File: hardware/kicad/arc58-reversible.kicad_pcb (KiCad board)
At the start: 2 copper layers, 169.3 x 152.2 mm, 91 parts, among them J1 MJ-4PP-9_Reversible, J2 SSD1306 OLED 128x32, SW1 SW_PUSH_LED, SW10 SW_PUSH_LED, SW11 SW_PUSH_LED, SW12 SW_PUSH_LED, SW13 SW_PUSH_LED, SW14 SW_PUSH_LED, SW15 SW_PUSH_LED, SW16 SW_PUSH_LED, SW17 SW_PUSH_LED, SW18 SW_PUSH_LED, SW19 SW_PUSH_LED, SW2 SW_PUSH_LED, SW20 SW_PUSH_LED, SW21 SW_PUSH_LED, SW22 SW_PUSH_LED, SW23 SW_PUSH_LED, SW24 SW_PUSH_LED, SW25 Rotary_Encoder_Switch, SW26 SW_PUSH_LED, SW27 SW_PUSH_LED, SW28 SW_PUSH_LED, SW29 SW_PUSH_LED, SW3 SW_PUSH_LED, SW4 SW_PUSH_LED, SW5 SW_PUSH_LED, SW6 SW_PUSH_LED, SW7 SW_PUSH_LED, SW8 SW_PUSH_LED, SW9 SW_PUSH_LED, U1 KEEBD Helios RP2040, U2 74AHCT1G125

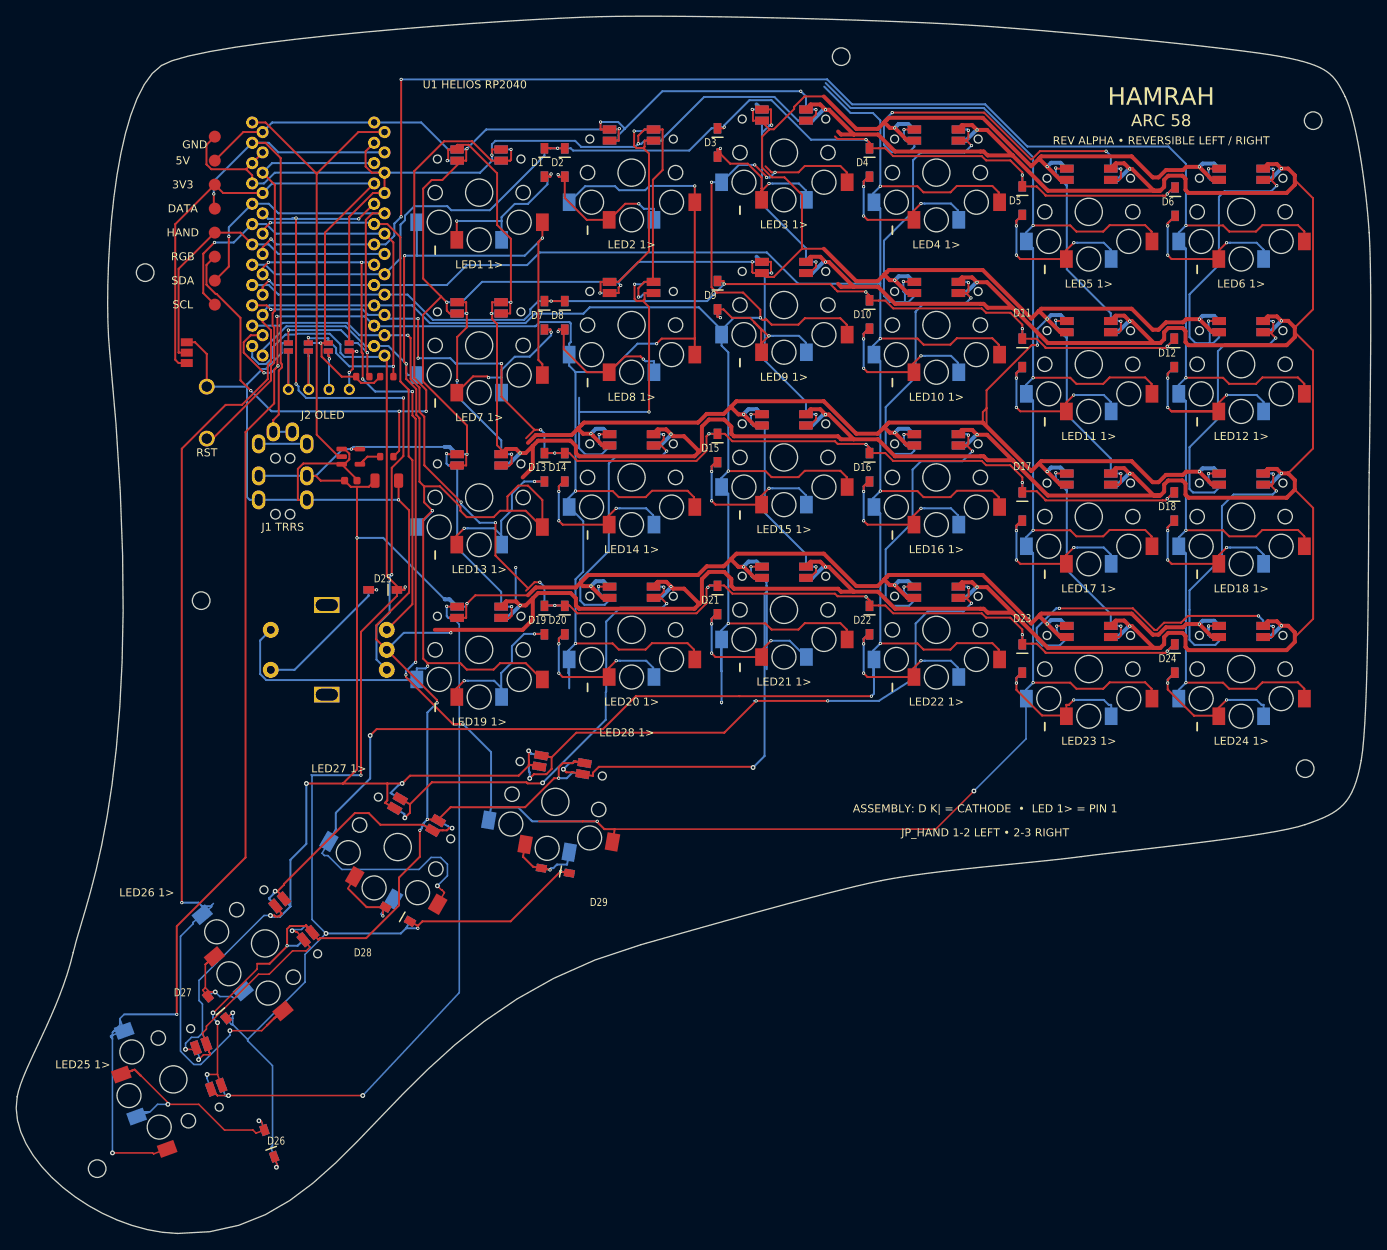
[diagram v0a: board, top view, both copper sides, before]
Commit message: Fix RGB apertures and TRRS clearance
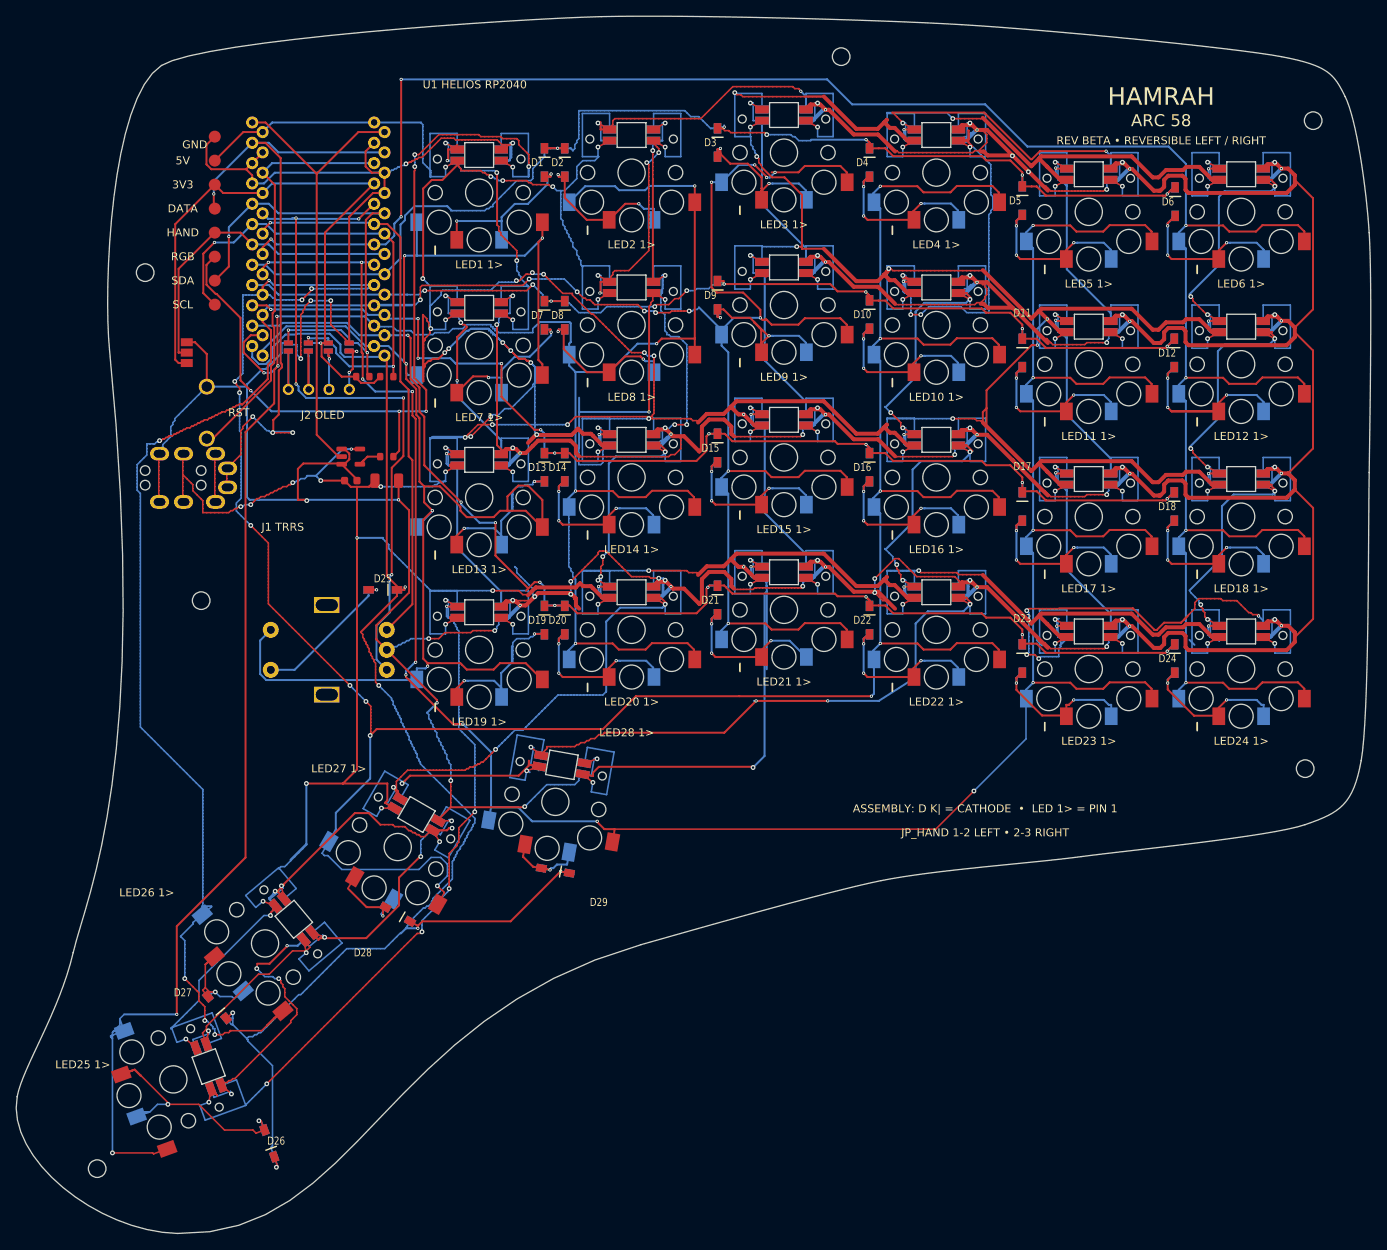
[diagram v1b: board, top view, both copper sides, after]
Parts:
- moved J1 12.7 mm to (83.3, 85.7), turned to 0 degrees
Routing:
- net VBUS: track 843.4 -> 1307.4 mm, vias 32 -> 73
- net GND: track 1032.1 -> 1181.9 mm, vias 35 -> 82
- net COL1: track 356.4 -> 310.9 mm
- net Net-(SW23-Pad2): track 45.4 -> 76.8 mm, vias 4 -> 7
- net Net-(SW10-Pad2): track 42.2 -> 71.2 mm, vias 3 -> 5
- net Net-(SW27-Pad2): track 36.5 -> 57.0 mm, vias 2 -> 4
- net RGB_LED_IN: track 96.4 -> 116.3 mm, vias 4 -> 7
- net Net-(SW14-Pad2): track 45.5 -> 64.1 mm, vias 3 -> 4
- net Net-(SW15-Pad2): track 27.7 -> 45.6 mm, vias 2 -> 3
- net Net-(SW11-Pad2): track 29.3 -> 46.3 mm, vias 2 -> 3
- net Net-(SW11-Pad4): track 29.3 -> 46.4 mm, vias 2 -> 3
- net Net-(SW17-Pad2): track 29.3 -> 46.3 mm, vias 2 -> 3
- net Net-(SW13-Pad2): track 27.9 -> 44.9 mm, vias 2 -> 3
- net SPLIT_DATA: track 68.8 -> 85.3 mm, vias 1 -> 4
- net Net-(SW1-Pad2): track 31.7 -> 47.7 mm, vias 2 -> 5
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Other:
- board text added: "REV BETA • REVERSIBLE LEFT / RIGHT"
- board text removed: "REV ALPHA • REVERSIBLE LEFT / RIGHT"

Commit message: Fix reversible thumb switch axes
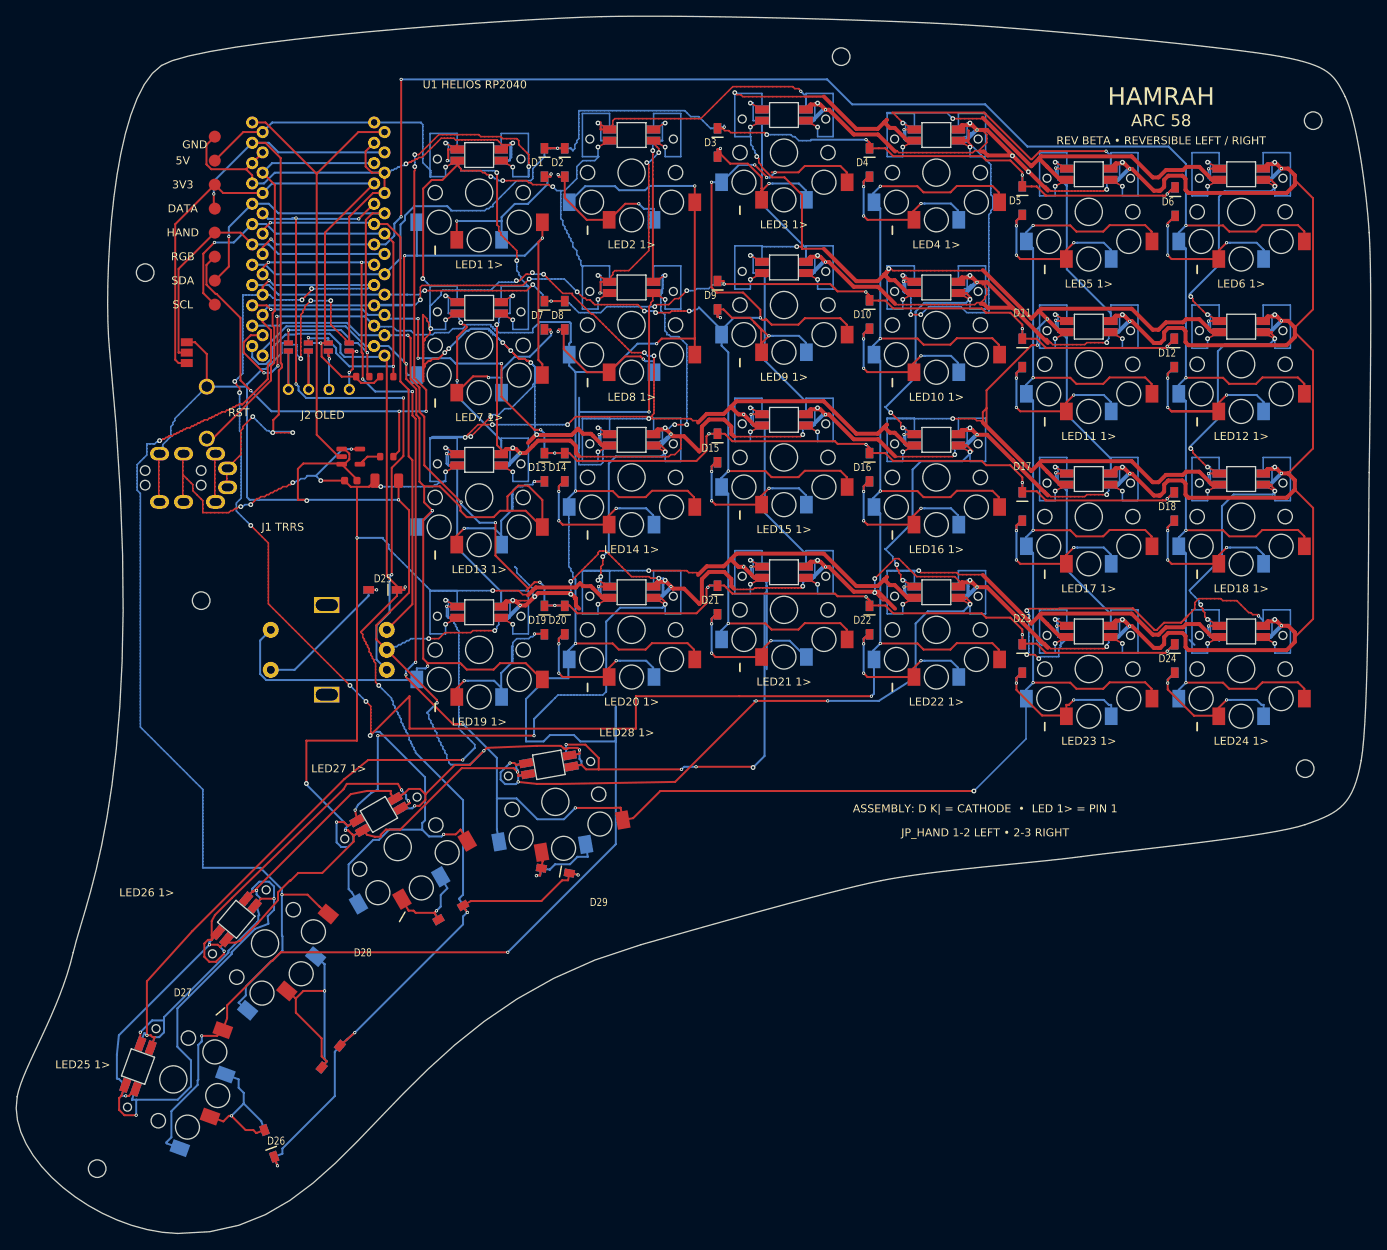
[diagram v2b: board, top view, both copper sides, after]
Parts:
- moved D27 15.5 mm to (102.0, 158.0), turned to -130 degrees
- moved D28 6.63 mm to (117.0, 140.0), turned to -150 degrees
- turned SW26 to -110 degrees
- turned SW27 to -130 degrees
- turned SW28 to -150 degrees
- turned SW29 to -170 degrees
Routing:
- net VBUS: track 1307.4 -> 1268.3 mm, vias 73 -> 71
- net ROW4: track 187.6 -> 168.7 mm
- net Net-(D26-Pad2): track 38.1 -> 19.7 mm, vias 2 -> 1
- net Net-(D27-Pad2): track 14.2 -> 30.7 mm
- net Net-(SW20-Pad4): track 76.0 -> 89.9 mm, vias 3 -> 5
- net Net-(SW26-Pad2): track 42.6 -> 56.0 mm
- net Net-(SW19-Pad2): track 103.3 -> 90.9 mm, vias 7 -> 4
- net Net-(SW27-Pad2): track 57.0 -> 47.8 mm, vias 4 -> 3
- net Net-(SW21-Pad2): track 83.5 -> 74.5 mm, vias 4 -> 6
- net GND: track 1181.9 -> 1175.4 mm, vias 82 -> 77
- net COL3: track 333.7 -> 327.7 mm, vias 17 -> 15
- net Net-(SW29-Pad2): track 91.8 -> 97.7 mm, vias 4 -> 5
- net COL2: track 341.6 -> 346.4 mm
- net COL4: track 314.2 -> 317.3 mm
- net Net-(D29-Pad2): track 12.3 -> 12.9 mm

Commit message: Clarify Helios handedness assembly
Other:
- board text added: "L"
- board text added: "L 1-2"
- board text added: "LEFT HELIOS • B.Cu FACE"
- board text added: "R"
- board text added: "R 2-3"
- board text added: "RIGHT HELIOS • F.Cu FACE"
- board text removed: "U1 HELIOS RP2040"
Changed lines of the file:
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@@
 		)
 	)
-	(gr_text "U1 HELIOS RP2040"
+	(gr_text "RIGHT HELIOS • F.Cu FACE"
 		(at 120 36.5 0)
+		(layer "F.SilkS")
+		(effects
+			(font
+				(size 1 1)
+				(thickness 0.15)
+			)
+		)
+	)
+	(gr_text "R"
+		(at 92.18 38.9 0)
+		(layer "F.SilkS")
+		(effects
+			(font
+				(size 1 1)
+				(thickness 0.15)
+			)
+		)
+	)
+	(gr_text "R"
+		(at 107.42 38.9 0)
+		(layer "F.SilkS")
+		(effects
+			(font
+				(size 1 1)
+				(thickness 0.15)
+			)
+		)
+	)
+	(gr_text "L 1-2"
+		(at 79.5 69.3 0)
+		(layer "F.SilkS")
+		(effects
+			(font
+				(size 1 1)
+				(thickness 0.15)
+			)
+		)
+	)
+	(gr_text "R 2-3"
+		(at 79.5 70.7 0)
 		(layer "F.SilkS")
 		(effects
@@
 		)
 	)
-	(gr_text "U1 HELIOS RP2040"
+	(gr_text "LEFT HELIOS • B.Cu FACE"
 		(at 120 36.5 0)
 		(layer "B.SilkS")
 		(effects
+			(font
+				(size 1 1)
+				(thickness 0.15)
+			)
+			(justify mirror)
+		)
+	)
+	(gr_text "L"
+		(at 93.479 40.1 0)
+		(layer "B.SilkS")
+		(effects
+			(font
+				(size 1 1)
+				(thickness 0.15)
+			)
+			(justify mirror)
+		)
+	)
+	(gr_text "L"
+		(at 108.719 40.1 0)
+		(layer "B.SilkS")
+		(effects

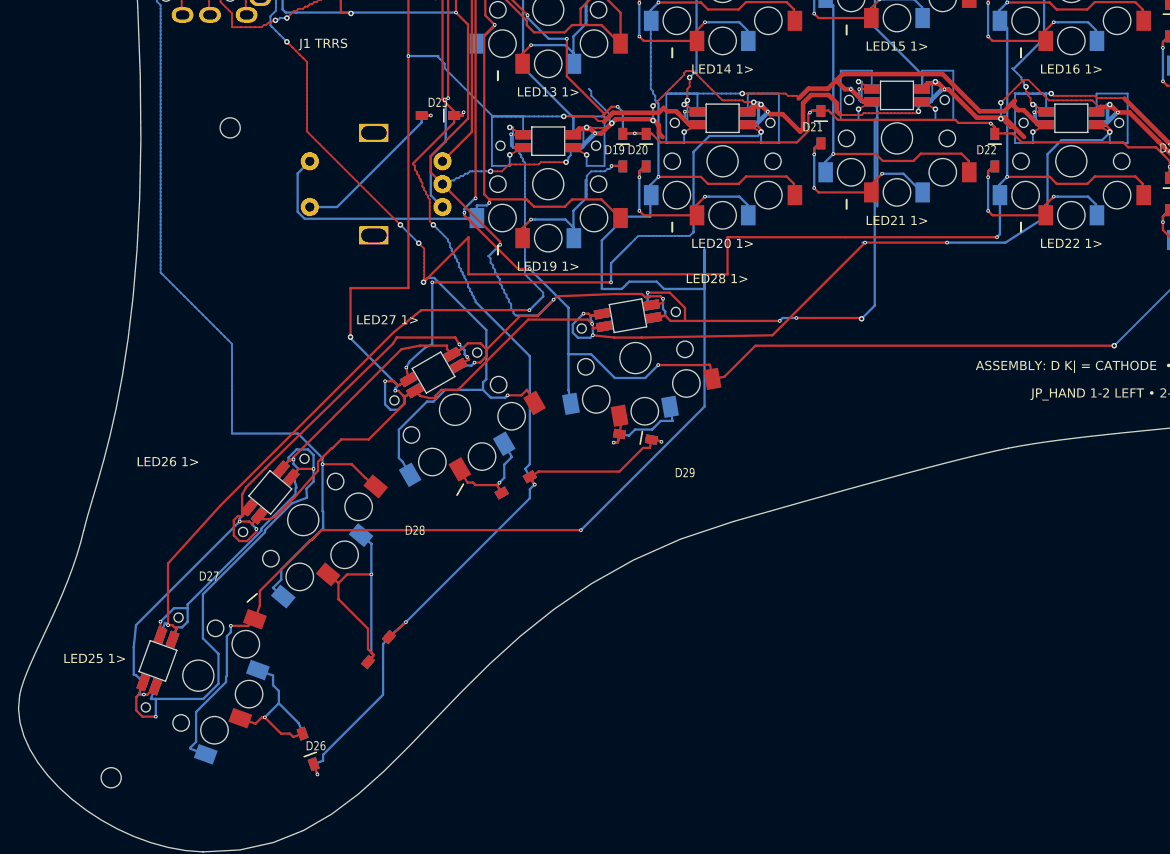
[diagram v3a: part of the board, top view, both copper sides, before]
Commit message: Fix thumb keycap clearance
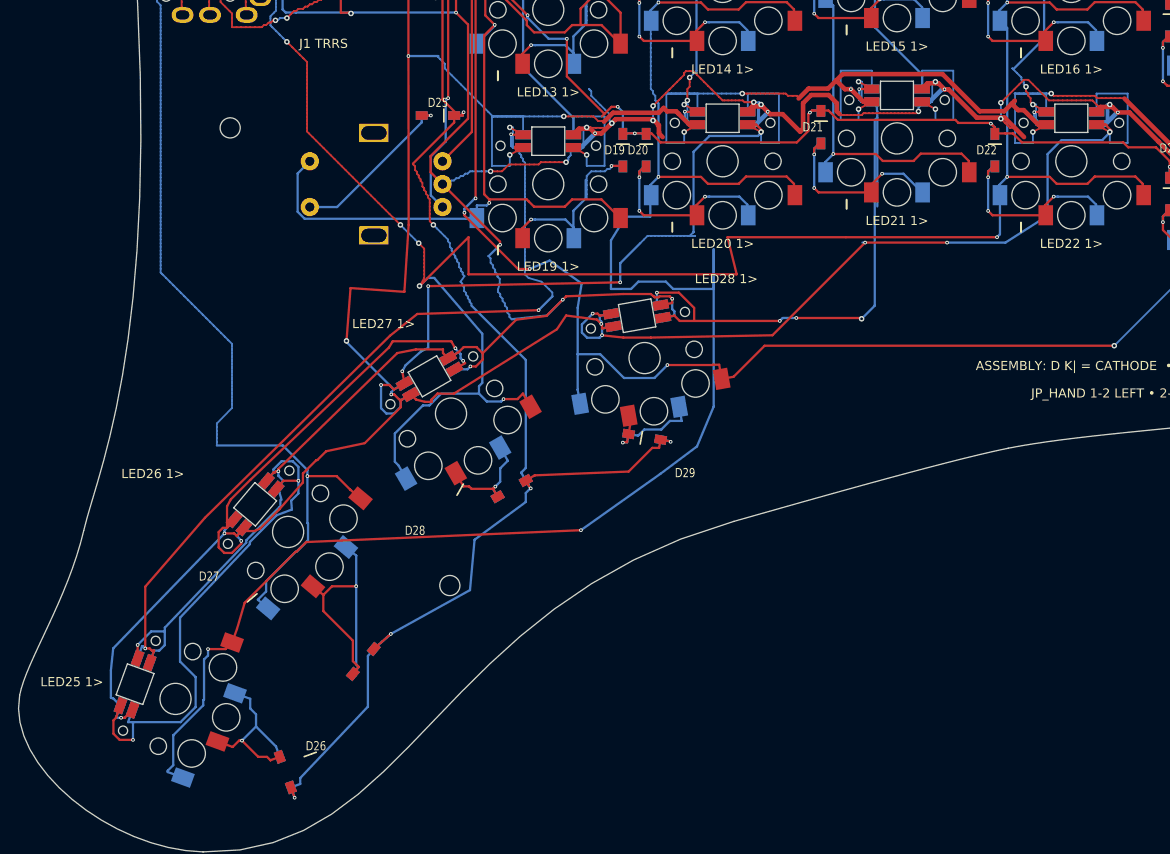
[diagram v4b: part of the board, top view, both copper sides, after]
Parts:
- moved H5 42.5 mm to (109.8, 151.0)
- moved D26 3.56 mm to (91.8, 171.4)
- moved SW26 3.56 mm to (79.8, 163.4)
- moved SW27 2.10 mm to (92.1, 145.1)
- moved D27 2.10 mm to (100.3, 159.3)
- moved SW29 1.00 mm to (131.1, 126.2)
- moved D29 1.00 mm to (131.1, 134.8)
- moved SW28 0.60 mm to (109.9, 132.2)
- moved D28 0.60 mm to (116.6, 140.4)
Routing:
- net ROW4: track 168.7 -> 175.4 mm
- net GND: track 1175.4 -> 1181.6 mm
- net Net-(SW19-Pad2): track 90.9 -> 96.2 mm
- net VBUS: track 1268.3 -> 1272.6 mm
- net COL4: track 317.3 -> 321.0 mm
- net COL2: track 346.4 -> 349.2 mm
- net COL1: track 311.0 -> 313.4 mm
- net COL3: track 327.7 -> 329.7 mm
- net Net-(SW20-Pad4): track 89.9 -> 91.5 mm
- net Net-(SW27-Pad2): track 47.8 -> 49.3 mm
- net Net-(SW26-Pad2): track 56.0 -> 57.5 mm
- net Net-(SW21-Pad2): track 74.5 -> 73.5 mm
- net Net-(SW29-Pad2): track 97.7 -> 96.7 mm
